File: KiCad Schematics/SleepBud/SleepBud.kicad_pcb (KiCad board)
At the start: 2 copper layers, 165 x 55 mm, 106 parts, among them J1 12V Barrel Jack, J2 USB_B_Micro, J3 Button Connector, J4 AM312 Connector, J5 LED Lamp Connector, J6 Connector to Buzzer, Q1 FQP27P06, Q2 AO3400A, SW1 EN Button, SW2 Reset Button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

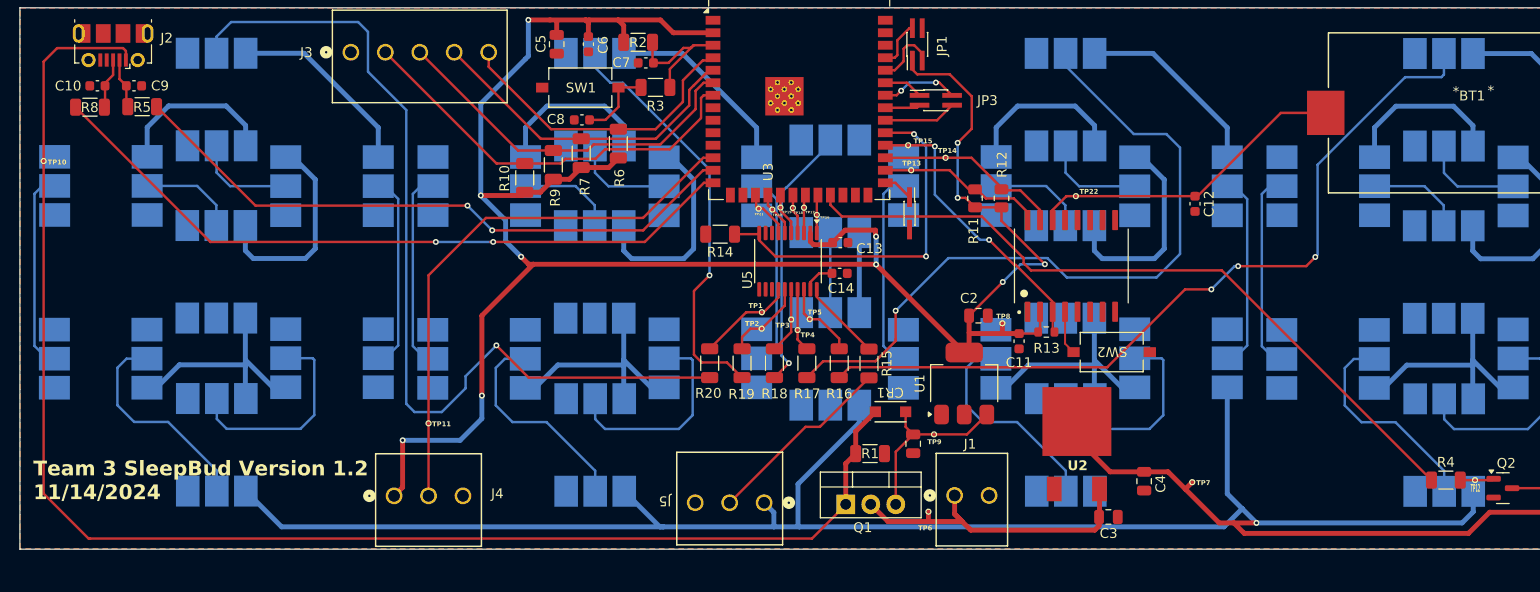
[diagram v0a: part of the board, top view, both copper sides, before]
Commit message: PCB Done Needs Checking Over
All NECESSARY warnings/errors are resolved just need checking with entire team/design review by others
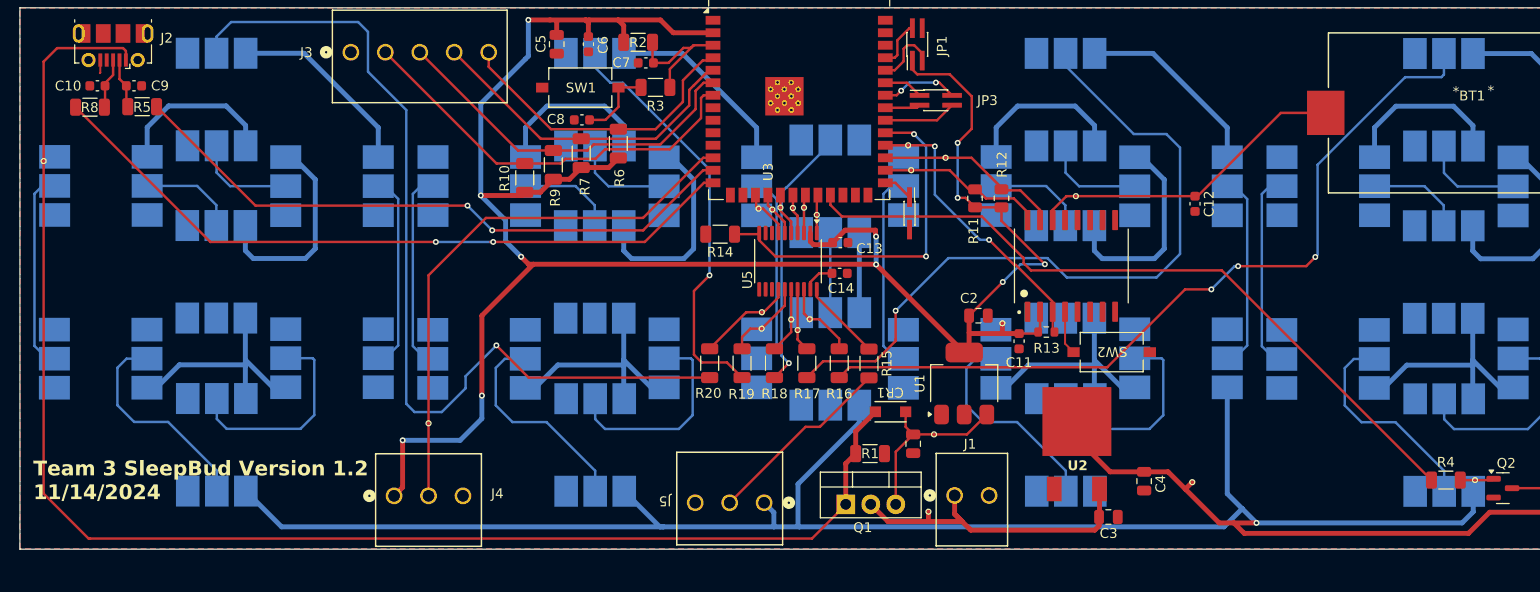
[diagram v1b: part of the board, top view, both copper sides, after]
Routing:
- net GND: track 0.00 -> 1.35 mm
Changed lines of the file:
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@@
 			(unlocked yes)
 			(layer "F.SilkS")
+			(hide yes)
 			(effects
 				(font
@@
 			(unlocked yes)
 			(layer "F.SilkS")
+			(hide yes)
 			(effects
 				(font
@@
 			(unlocked yes)
 			(layer "F.SilkS")
+			(hide yes)
 			(effects
 				(font
@@
 			(unlocked yes)
 			(layer "F.SilkS")
+			(hide yes)
 			(effects
 				(font
@@
 			(unlocked yes)
 			(layer "F.SilkS")
+			(hide yes)
 			(effects
 				(font
@@
 			(unlocked yes)
 			(layer "F.SilkS")
+			(hide yes)
 			(effects
 				(font
@@
 			(unlocked yes)
 			(layer "F.SilkS")
+			(hide yes)
 			(effects
 				(font
@@
 			(unlocked yes)
 			(layer "F.SilkS")
+			(hide yes)
 			(effects
 				(font
@@
 			(unlocked yes)
 			(layer "F.SilkS")
+			(hide yes)
 			(effects
 				(font
@@
 			(unlocked yes)
 			(layer "F.SilkS")
+			(hide yes)
 			(effects
 				(font
@@
 			(unlocked yes)
 			(layer "F.SilkS")
+			(hide yes)
 			(effects
 				(font
@@
 			(unlocked yes)
 			(layer "F.SilkS")
+			(hide yes)
 			(effects
 				(font
@@
 		(at 149.51 107.54)
 		(property "Reference" "TP6"
-			(at -0.43 -0.69 0)
+			(at -0.9 0.15 0)
 			(unlocked yes)
 			(layer "F.SilkS")
+			(hide yes)
 			(effects
 				(font
-					(size 0.5 0.5)
+					(size 0.8 0.8)
 					(thickness 0.125)
 					(bold yes)
@@
 			(unlocked yes)
 			(layer "F.SilkS")
+			(hide yes)
 			(effects
 				(font
@@
 			(unlocked yes)
 			(layer "F.SilkS")
+			(hide yes)
 			(effects
 				(font
@@
 			(unlocked yes)
 			(layer "F.SilkS")
+			(hide yes)
 			(effects
 				(font
@@
 			(unlocked yes)
 			(layer "F.SilkS")
+			(hide yes)
 			(effects
 				(font
@@
 			(unlocked yes)
 			(layer "F.SilkS")
+			(hide yes)
 			(effects
 				(font
@@
 			(unlocked yes)
 			(layer "F.SilkS")
+			(hide yes)
 			(effects
 				(font
@@
 		(at 132.26 76.76)
 		(property "Reference" "TP21"
-			(at -0.07 -1.79 0)
+			(at -0.06 -1.51 0)
 			(unlocked yes)
 			(layer "F.SilkS")
+			(hide yes)
 			(effects
 				(font
-					(size 0.25 0.25)
-					(thickness 0.0625)
+					(size 0.8 0.6)
+					(thickness 0.127)
 					(bold yes)
 				)
@@
 			(unlocked yes)
 			(layer "F.SilkS")
+			(hide yes)
 			(effects
 				(font
@@
 			(unlocked yes)
 			(layer "F.SilkS")
+			(hide yes)
 			(effects
 				(font
@@
 	)
 	(segment
+		(start 65.29 59.3125)
+		(end 65.29 60.59)
+		(width 0.2)
+		(layer "F.Cu")
+		(net 2)
+	)
+	(segment
+		(start 65.29 60.59)
+		(end 65.24 60.64)
+		(width 0.2)
+		(layer "F.Cu")
+		(net 2)
+	)
+	(segment

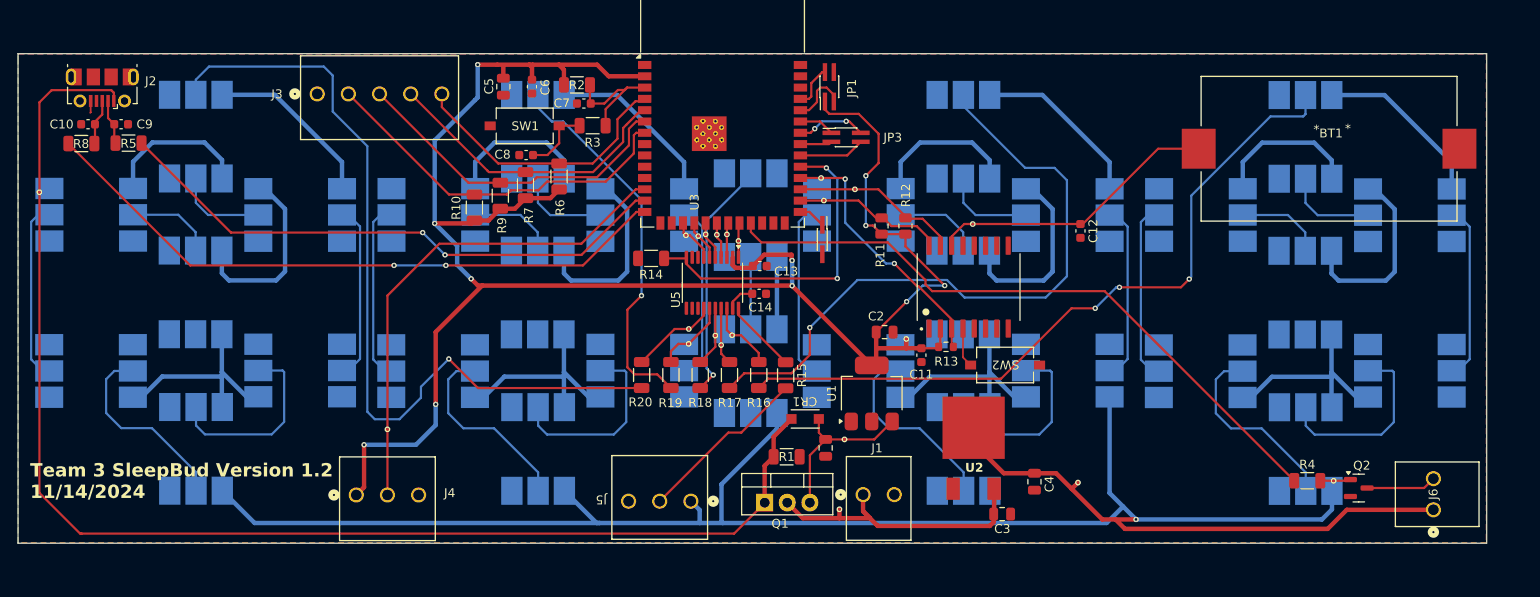
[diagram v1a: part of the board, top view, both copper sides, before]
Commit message: Changed PMosfet
Change the Mosfet can be seen on schematic and PCB layout
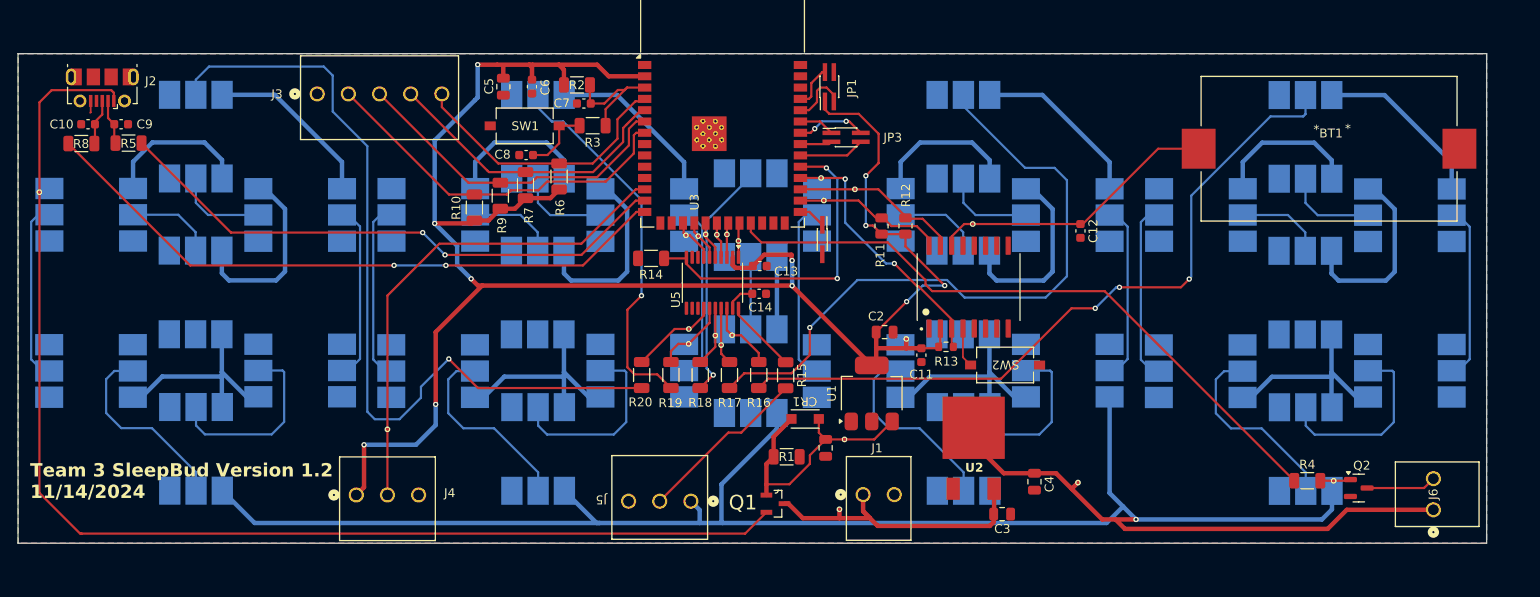
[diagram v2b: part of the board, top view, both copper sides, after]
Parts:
- Q1: value FQP27P06 -> DMG3415U-7; footprint Package_TO_SOT_THT:TO-220-3_Vertical -> DMG3415U_7:SOT95P240X105-3N
- moved Q1 1.22 mm to (142.2, 104.6)
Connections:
- C1 pad 1: Net-(Q1-S) -> VBUS
- CR1 pad 1: Net-(Q1-S) -> VBUS
- Q1 pad 2: +12V -> VBUS
- Q1 pad 3: Net-(Q1-S) -> +12V
- TP9 pad 1: Net-(Q1-S) -> VBUS
- U1 pad 3: Net-(Q1-S) -> VBUS
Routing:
- net VBUS: track 149.6 -> 168.6 mm
- net Net-(Q1-S): track 18.8 -> 0.00 mm

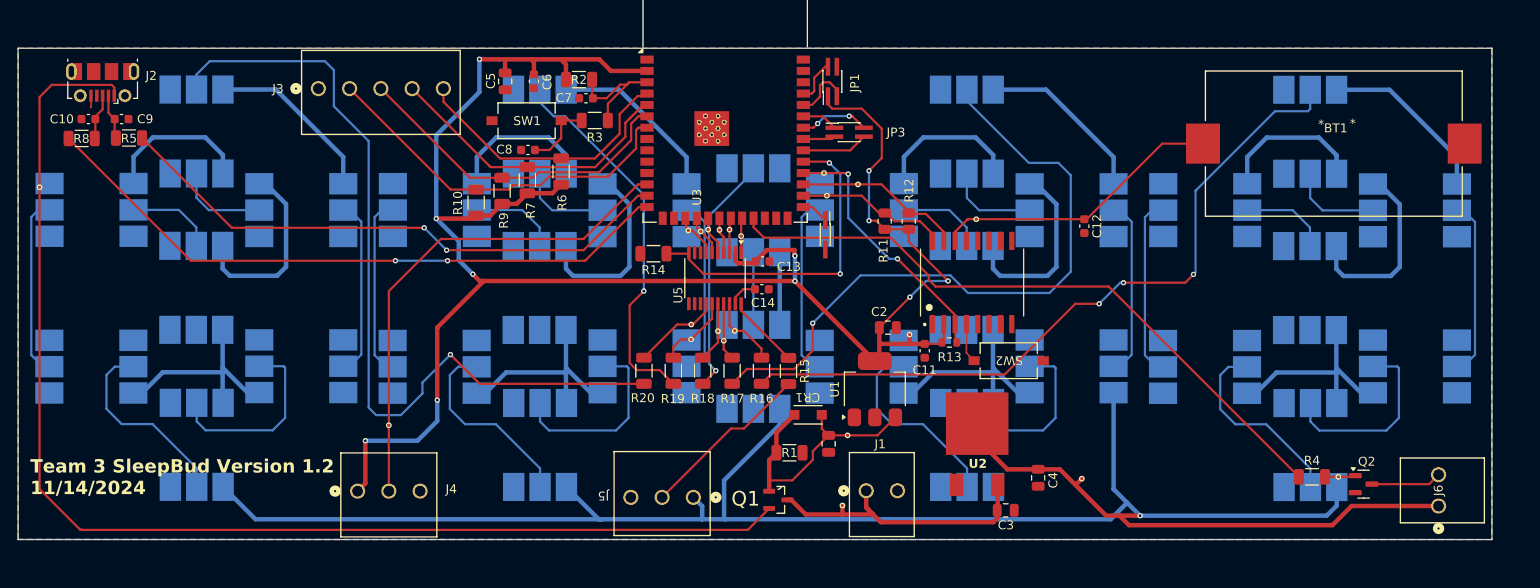
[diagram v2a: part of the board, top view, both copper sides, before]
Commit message: Added Some Ground Vias to each Corner of the Board
Still missing the ground stitching for some components, will work on it it later
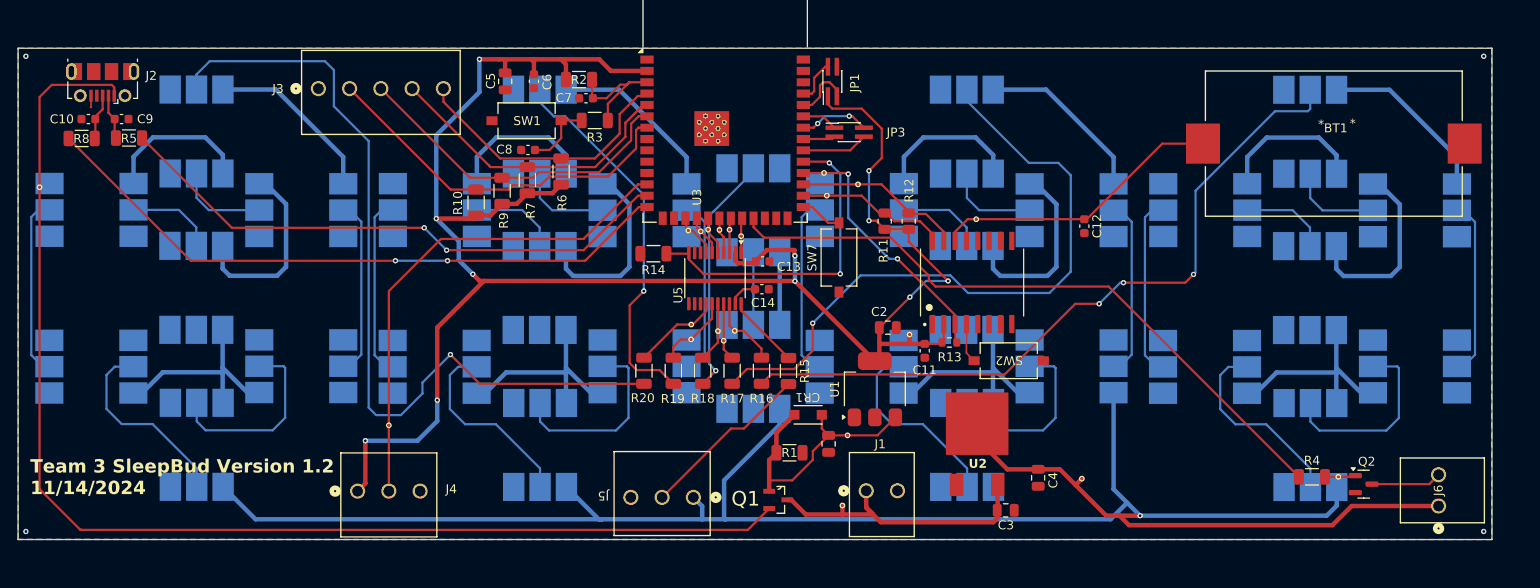
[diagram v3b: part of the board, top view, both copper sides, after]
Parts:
- removed JP2: Boot Option, Connector_PinHeader_1.00mm:PinHeader_2x01_P1.00mm_Vertical_SMD
- added SW7: Boot Button, Button_Switch_SMD:SW_Tactile_SPST_NO_Straight_CK_PTS636Sx25SMTRLFS, F.Cu at (149.0, 77.4)
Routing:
- net Net-(U3-IO0): track 3.06 -> 4.72 mm
- net GND: vias 0 -> 4

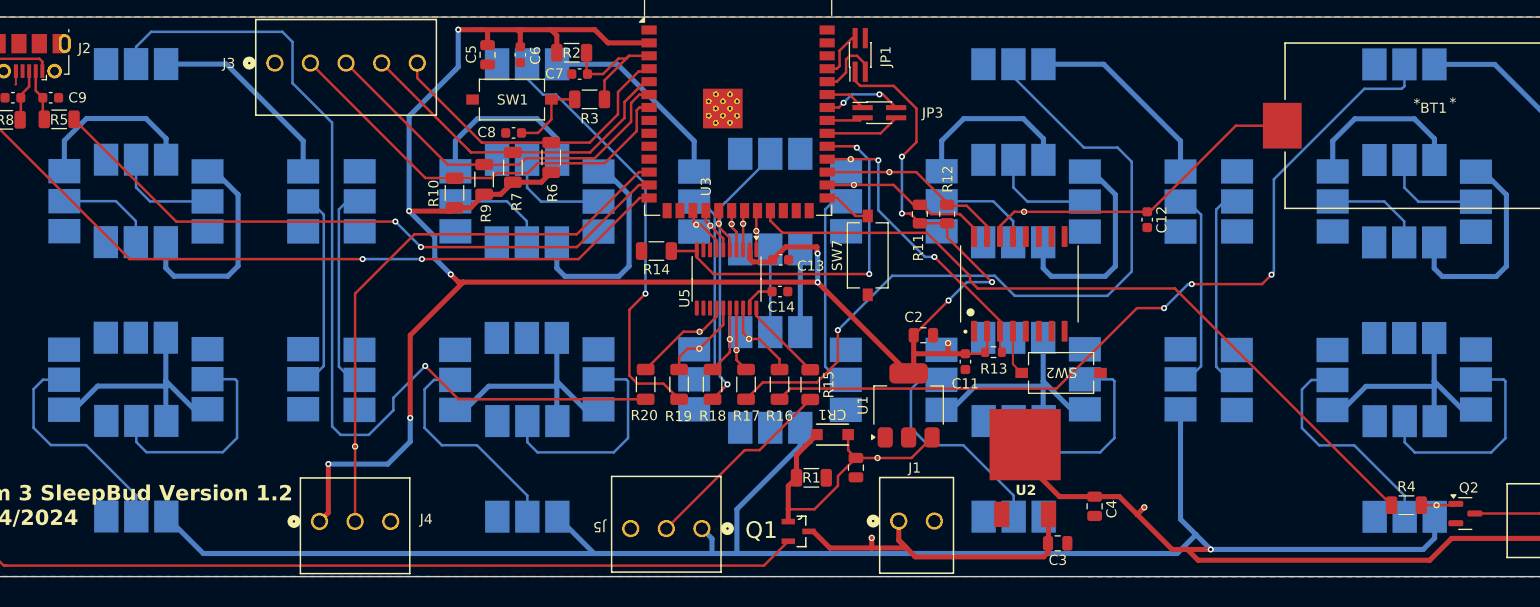
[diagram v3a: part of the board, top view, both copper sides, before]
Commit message: Added Some More Ground Vias
I think I did the ground stitching correctly, need team to check if its correct.
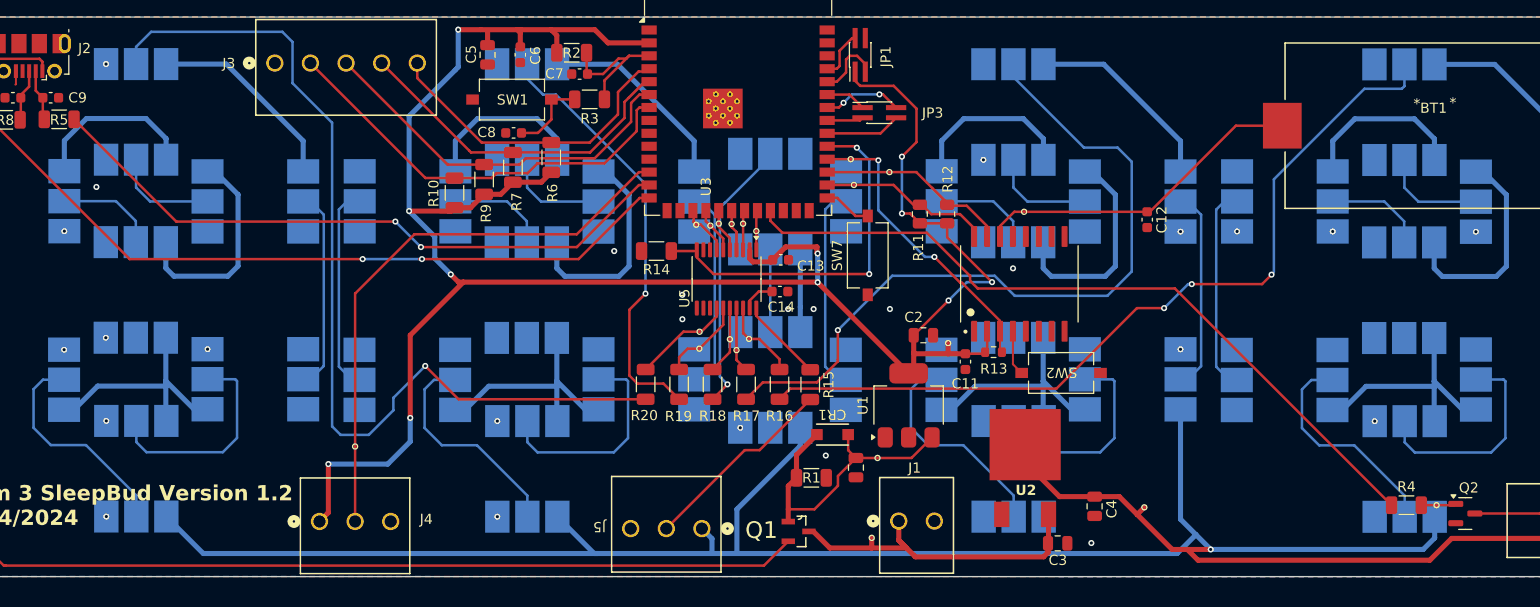
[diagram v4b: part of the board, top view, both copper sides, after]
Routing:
- net GND: vias 4 -> 31
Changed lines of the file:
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@@
+	)
+	(via
+		(at 143.7 82.7)
+		(size 0.6)
+		(drill 0.3)
+		(layers "F.Cu" "B.Cu")
+		(free yes)
+		(net 2)
+	)
+	(via
+		(at 112.61 103.1125)
+		(size 0.6)
+		(drill 0.3)
+		(layers "F.Cu" "B.Cu")
+		(net 2)
+	)
+	(via
+		(at 198.85 93.725)
+		(size 0.6)
+		(drill 0.3)
+		(layers "F.Cu" "B.Cu")
+		(net 2)
+	)
+	(via
+		(at 74.175 103.0975)
+		(size 0.6)
+		(drill 0.3)
+		(layers "F.Cu" "B.Cu")
+		(net 2)
 	)
 	(via
@@
 	)
 	(via
+		(at 70.025 86.6975)
+		(size 0.6)
+		(drill 0.3)
+		(layers "F.Cu" "B.Cu")
+		(net 2)
+	)
+	(via
+		(at 73.2 70.7)
+		(size 0.6)
+		(drill 0.3)
+		(layers "F.Cu" "B.Cu")
+		(free yes)
+		(net 2)
+	)
+	(via
+		(at 171 105.7)
+		(size 0.6)
+		(drill 0.3)
+		(layers "F.Cu" "B.Cu")
+		(free yes)
+		(net 2)
+	)
+	(via
+		(at 130.8 83.7)
+		(size 0.6)
+		(drill 0.3)
+		(layers "F.Cu" "B.Cu")
+		(free yes)
+		(net 2)
+	)
+	(via
+		(at 74.175 93.6975)
+		(size 0.6)
+		(drill 0.3)
+		(layers "F.Cu" "B.Cu")
+		(net 2)
+	)
+	(via
+		(at 84.125 86.6475)
+		(size 0.6)
+		(drill 0.3)
+		(layers "F.Cu" "B.Cu")
+		(net 2)
+	)
+	(via
+		(at 151.2 82.7)
+		(size 0.6)
+		(drill 0.3)
+		(layers "F.Cu" "B.Cu")
+		(free yes)
+		(net 2)
+	)
+	(via
+		(at 194.725 75.075)
+		(size 0.6)
+		(drill 0.3)
+		(layers "F.Cu" "B.Cu")
+		(net 2)
+	)
+	(via
+		(at 163.3 78.7)
+		(size 0.6)
+		(drill 0.3)
+		(layers "F.Cu" "B.Cu")
+		(free yes)
+		(net 2)
+	)
+	(via
+		(at 144.9 97.1)
+		(size 0.6)
+		(drill 0.3)
+		(layers "F.Cu" "B.Cu")
+		(free yes)
+		(net 2)
+	)
+	(via
+		(at 141.2 82.7)
+		(size 0.6)
+		(drill 0.3)
+		(layers "F.Cu" "B.Cu")
+		(free yes)
+		(net 2)
+	)
+	(via
+		(at 74.15 58.6225)
+		(size 0.6)
+		(drill 0.3)
+		(layers "F.Cu" "B.Cu")
+		(net 2)
+	)
+	(via
+		(at 112.61 93.7125)
+		(size 0.6)
+		(drill 0.3)
+		(layers "F.Cu" "B.Cu")
+		(net 2)
+	)
+	(via
+		(at 70.05 75.0475)
+		(size 0.6)
+		(drill 0.3)
+		(layers "F.Cu" "B.Cu")
+		(net 2)
+	)
+	(via
+		(at 136.49 94.37)
+		(size 0.6)
+		(drill 0.3)
+		(layers "F.Cu" "B.Cu")
+		(net 2)
+	)
+	(via
+		(at 124.1 77)
+		(size 0.6)
+		(drill 0.3)
+		(layers "F.Cu" "B.Cu")
+		(free yes)
+		(net 2)
+	)
+	(via
 		(at 221.2 108.1)
 		(size 0.6)
@@
 	)
 	(via
+		(at 208.8 75.1)
+		(size 0.6)
+		(drill 0.3)
+		(layers "F.Cu" "B.Cu")
+		(net 2)
+	)
+	(via
+		(at 185.325 75.075)
+		(size 0.6)
+		(drill 0.3)
+		(layers "F.Cu" "B.Cu")
+		(net 2)
+	)
+	(via
 		(at 58 108.1)
 		(size 0.6)
@@
 	)
 	(via
+		(at 160.39 68.035)
+		(size 0.6)
+		(drill 0.3)
+		(layers "F.Cu" "B.Cu")
+		(net 2)
+	)
+	(via
+		(at 179.765 75.085)
+		(size 0.6)
+		(drill 0.3)
+		(layers "F.Cu" "B.Cu")
+		(net 2)
+	)
+	(via
+		(at 74.125 85.5225)
+		(size 0.6)
+		(drill 0.3)
+		(layers "F.Cu" "B.Cu")
+		(net 2)
+	)
+	(via
+		(at 179.765 86.66)
+		(size 0.6)
+		(drill 0.3)
+		(layers "F.Cu" "B.Cu")
+		(net 2)
+	)
+	(via
 		(at 221.2 54.9)
+		(size 0.6)
+		(drill 0.3)
+		(layers "F.Cu" "B.Cu")
+		(free yes)
+		(net 2)
+	)
+	(via
+		(at 130.8 81.3)
 		(size 0.6)
 		(drill 0.3)
@@
 	)
 	(segment
+		(start 142.39 82.5)
+		(end 142.39 84.97)
+		(width 0.5)
+		(layer "B.Cu")
+		(net 5)
+	)
+	(segment
 		(start 118.46 89.7875)
 		(end 118.46 90.3875)
@@
 	(segment
 		(start 142.39 76.84)
-		(end 142.39 84.97)
-		(width 0.5)
-		(layer "B.Cu")
+		(end 142.39 82.5)
+		(width 0.5)
+		(layer "B.Cu")
